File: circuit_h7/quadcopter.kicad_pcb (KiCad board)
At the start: 4 copper layers, 37.5 x 37.5 mm, 105 parts, among them J10 Conn_01x01_Female, J11 Conn_01x04_Male, J12 Conn_01x04_Male, J13 Conn_01x01_Female, J16 Conn_01x01_Female, J17 Conn_01x01_Female, J18 USB_C_Receptacle_USB2.0, J19 Conn_01x08_Male, J21 Conn_01x01_Female, J22 Conn_01x01_Female, J23 Conn_01x01_Female, J24 Conn_01x01_Female, J25 Conn_01x01_Female, J26 Conn_01x01_Female, J28 Conn_01x01_Female, J29 Conn_01x01_Female, J3 Conn_01x01_Female, J30 Conn_01x01_Female, J31 Conn_01x01_Female, J32 Conn_01x01_Female, J33 Conn_01x01_Female, J37 Conn_01x01_Female, J4 Conn_01x01_Female, J40 Conn_01x01_Female, J41 Conn_01x01_Female, J42 Conn_01x01_Female, J43 Conn_01x01_Female, J44 Conn_01x01_Female, J45 Conn_01x01_Female, J47 Conn_01x01_Female, J48 Conn_01x01_Female, J49 Conn_01x01_Female, J5 Conn_Coaxial, J50 Conn_01x01_Female, J6 Conn_01x06_Male, J7 Conn_01x01_Female, J8 Conn_01x01_Female, J9 Conn_01x01_Female, SW1 SW_DIP_x01, U1 STM32F103VDHx, U2 ICM-42605, U3 DPS310, U4 3V3, U5 EUP3458 1.2A, 30V max input, 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, U6 2450FM07D0034T, U7 W25Q80DVUXIE TR (16M), U8 SX1281, U9 5v, 500mA, Y1 16M, Y2 52Mhz, 12pF

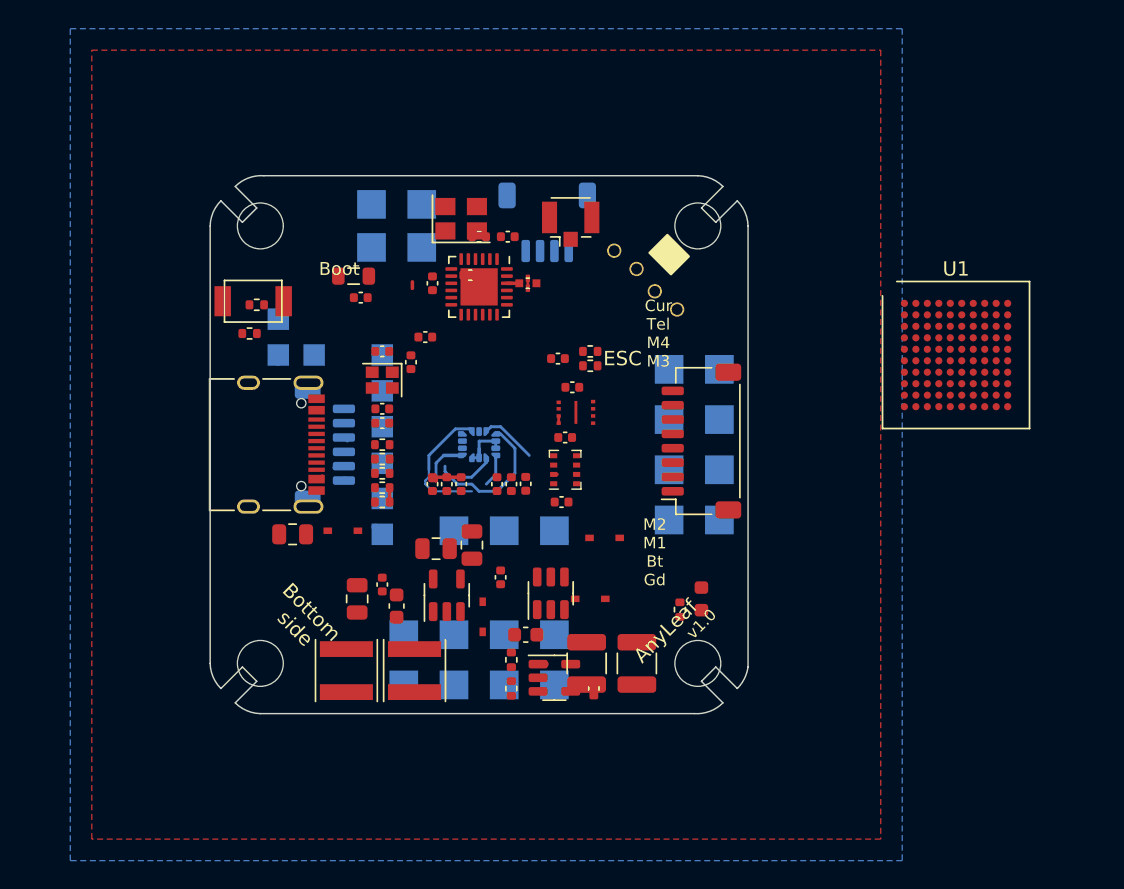
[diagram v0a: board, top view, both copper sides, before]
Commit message: More work on H7 board layout
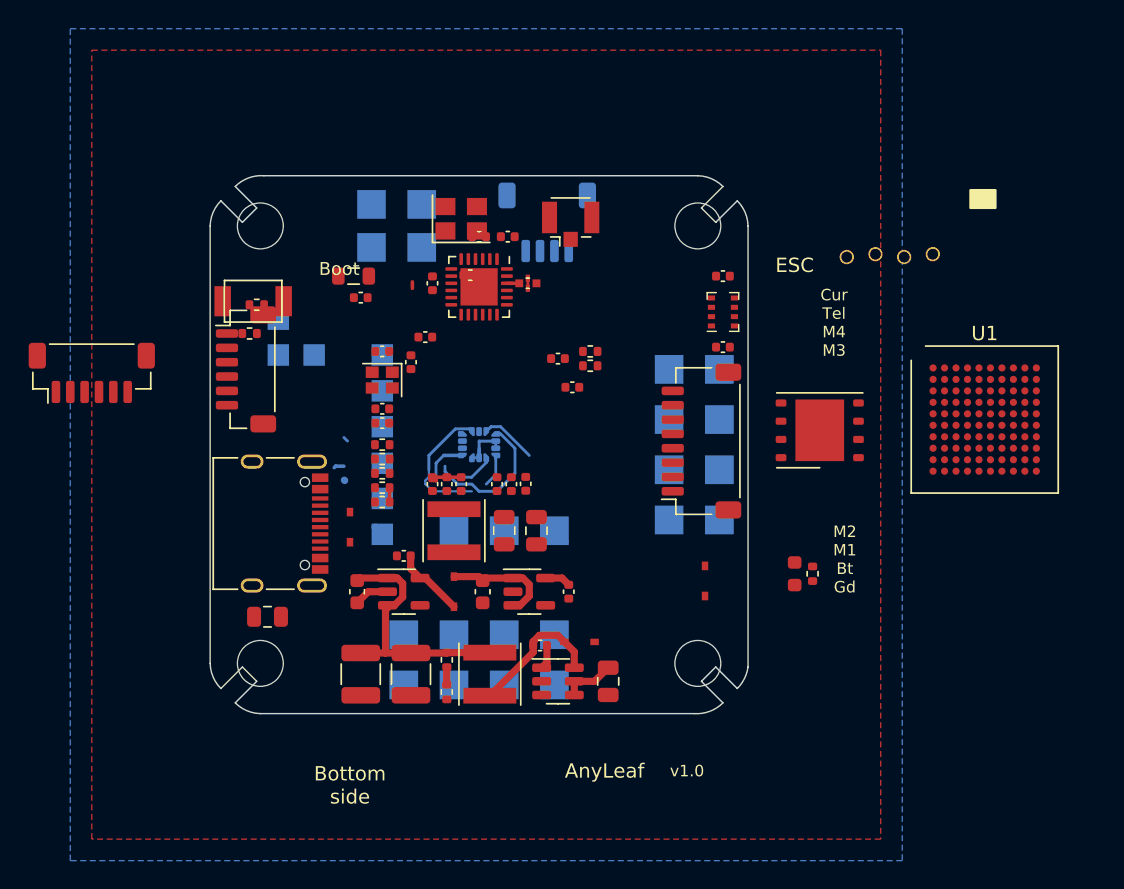
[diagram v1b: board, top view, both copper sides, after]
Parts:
- added J1: Conn_01x06_Male, Connector_JST:JST_SH_BM06B-SRSS-TB_1x06-1MP_P1.00mm_Vertical, F.Cu at (110.0, 82.5)
- J6: moved to F.Cu
- U7: footprint Anyleaf_Shared:USON-8_2.0x3.0mm_P0.5mm -> Package_SON:WSON-8-1EP_6x5mm_P1.27mm_EP3.4x4.3mm
- moved C24 19.3 mm to (128.8, 103.5)
- moved U7 17.0 mm to (160.8, 86.5)
- moved C22 16.2 mm to (131.8, 95.2), turned to 0 degrees
- moved C2 15.7 mm to (154.0, 75.8)
- moved C5 15.6 mm to (154.0, 80.7)
- moved U3 15.6 mm to (154.0, 78.2)
- moved C14 13.4 mm to (146.0, 104.0)
- moved C31 13.4 mm to (141.0, 93.5), turned to 90 degrees
- moved C8 13.0 mm to (143.2, 97.8), turned to 90 degrees
- moved J12 12.4 mm to (162.6, 74.4), turned to 0 degrees
- moved L1 12.3 mm to (135.2, 93.5)
- moved C20 12.3 mm to (132.2, 103.5)
- moved C15 12.1 mm to (128.5, 97.8), turned to 90 degrees
- moved U9 12.1 mm to (131.8, 97.8)
- moved R12 9.58 mm to (160.2, 96.5)
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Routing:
- net +10V: track 1.24 -> 18.8 mm
- net Net-(C21-Pad2): track 0.00 -> 9.66 mm
- net +5V: track 1.83 -> 9.66 mm
- net Net-(C22-Pad2): track 0.00 -> 5.01 mm
- net +BATT: track 0.00 -> 3.71 mm
- net GND: track 5.93 -> 8.60 mm
- net Net-(C21-Pad1): track 0.00 -> 1.70 mm
- net Net-(R7-Pad1): track 0.00 -> 1.23 mm
- net +3V3: track 1.43 -> 2.30 mm

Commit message: refactored state into sep module; moved some code to statevolatile that were individual resources.
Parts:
- added J14: Conn_01x01_Female, TestPoint:TestPoint_Pad_2.0x2.0mm, B.Cu at (128.2, 100.8)
- added J2: Conn_01x01_Female, TestPoint:TestPoint_Pad_2.0x2.0mm, B.Cu at (128.2, 104.2)
- U1: footprint Package_BGA:LFBGA-100_10x10mm_Layout10x10_P0.8mm -> Package_BGA:TFBGA-100_8x8mm_Layout10x10_P0.8mm
- moved C11 46.9 mm to (178.2, 93.2)
- moved C16 45.9 mm to (176.0, 95.5)
- moved R13 45.8 mm to (174.0, 105.0)
- moved R14 45.8 mm to (174.0, 104.0)
- moved C10 39.2 mm to (179.2, 95.2)
- moved R16 39.0 mm to (174.0, 107.8)
- moved R18 39.0 mm to (174.0, 106.8)
- moved U1 35.3 mm to (137.0, 84.2)
- moved D3 29.1 mm to (147.5, 69.8), turned to 180 degrees
- moved R12 28.3 mm to (147.5, 71.2), turned to 0 degrees
- moved C18 27.2 mm to (146.5, 64.2)
- moved R2 15.2 mm to (128.0, 91.5), turned to 0 degrees
- moved U7 14.4 mm to (148.8, 78.5), turned to 0 degrees
- moved J33 12.8 mm to (142.2, 104.2)
- moved C25 12.1 mm to (150.0, 98.0)
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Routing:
- net /V_DCC: track 0.00 -> 22.1 mm
- net +3V3: track 2.30 -> 15.3 mm
- net +BATT: track 3.71 -> 13.9 mm
- net /BAT_IN: track 0.00 -> 9.18 mm
- net /IMU_pwr: track 8.71 -> 14.7 mm
- net Net-(F1-Pad2): track 0.00 -> 5.24 mm
- net Net-(U8-Pad6): track 0.85 -> 5.84 mm
- net Net-(U8-Pad4): track 0.00 -> 4.82 mm
- net /V_DCC2: track 0.00 -> 3.54 mm
- net Net-(J5-Pad1): track 0.00 -> 2.16 mm
- net Net-(C19-Pad2): track 0.00 -> 1.67 mm
- net Net-(J18-PadB5): track 0.00 -> 1.67 mm
- net Net-(J18-PadA7): track 0.00 -> 1.67 mm
- net Net-(J18-PadA6): track 0.00 -> 1.67 mm
- net Net-(J18-PadA5): track 0.00 -> 1.67 mm
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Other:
- board text added: "5"
- board text added: "Mercury H7"
- board text removed: "Mercury G4"
